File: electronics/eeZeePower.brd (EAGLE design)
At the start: 20.3 x 11.6 mm, 10 parts

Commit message: Updated version #
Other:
- board text added: "R0.6"
- board text removed: "R0.5"
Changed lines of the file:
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@@
 <text x="5.334" y="1.651" size="1.27" layer="27" font="vector">eeZee Power</text>
 <text x="5.334" y="0.508" size="1.016" layer="21" font="vector">bot-thoughts.com</text>
-<text x="19.939" y="4.318" size="0.8128" layer="21" font="vector" rot="R90">R0.5</text>
+<text x="19.939" y="4.318" size="0.8128" layer="21" font="vector" rot="R90">R0.6</text>
 <text x="11.176" y="7.493" size="1.016" layer="27" font="vector" rot="R180">VCC</text>
 <text x="11.176" y="4.953" size="1.016" layer="27" font="vector" rot="R180">GND</text>

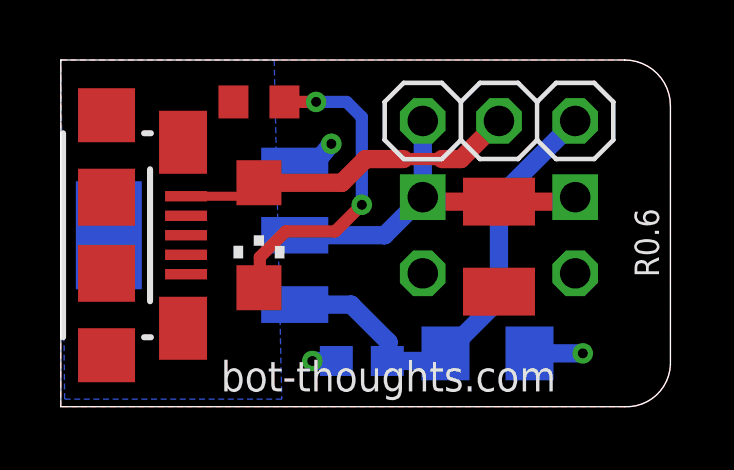
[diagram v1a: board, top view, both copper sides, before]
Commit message: updated silk, updated board name to microB
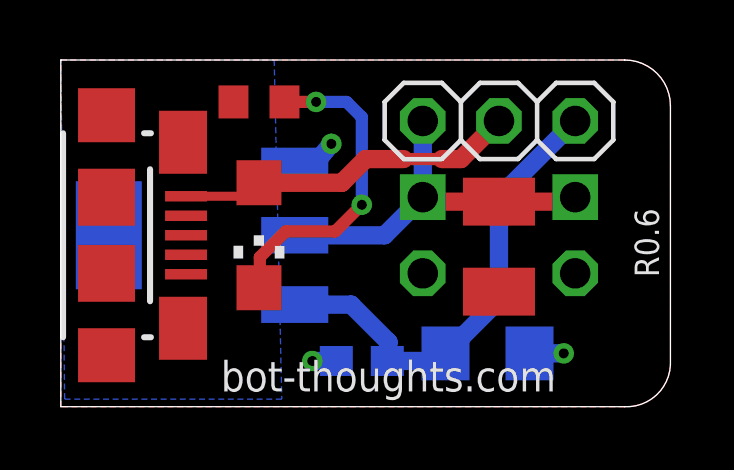
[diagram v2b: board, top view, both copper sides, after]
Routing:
- net GND: track 4.14 -> 3.51 mm
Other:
- board text added: "eeZeePowerμB"
- board text removed: "eeZee Power"
- board text removed: "μB"
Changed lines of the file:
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@@
 <wire x1="0" y1="11.557" x2="0" y2="0" width="0" layer="20"/>
 <text x="10.541" y="8.636" size="1.016" layer="27" font="vector" rot="R90">VU</text>
-<text x="5.334" y="1.651" size="1.27" layer="27" font="vector">eeZee Power</text>
+<text x="5.334" y="1.651" size="1.27" layer="27" font="vector">eeZeePowerμB</text>
 <text x="5.334" y="0.508" size="1.016" layer="21" font="vector">bot-thoughts.com</text>
 <text x="19.939" y="4.318" size="0.8128" layer="21" font="vector" rot="R90">R0.6</text>
@@
 <text x="11.176" y="4.953" size="1.016" layer="27" font="vector" rot="R180">GND</text>
 <text x="18.669" y="10.795" size="1.016" layer="27" font="vector" rot="R270">3V3</text>
-<text x="17.907" y="1.778" size="1.27" layer="27" font="vector">μB</text>
 </plain>
 <attributes>
@@
 <contactref element="JP1" pad="GND"/>
 <wire x1="9.183" y1="1.524" x2="8.382" y2="1.524" width="0.6096" layer="16"/>
-<wire x1="15.624" y1="1.778" x2="17.399" y2="1.778" width="0.6096" layer="16"/>
+<wire x1="15.624" y1="1.778" x2="16.764" y2="1.778" width="0.6096" layer="16"/>
 <via x="8.382" y="1.524" extent="1-16" drill="0.3302"/>
-<via x="17.399" y="1.778" extent="1-16" drill="0.3302"/>
+<via x="16.764" y="1.778" extent="1-16" drill="0.3302"/>
 <wire x1="7.7978" y1="8.0264" x2="8.4074" y2="8.0264" width="0.6096" layer="16"/>
 <wire x1="8.4074" y1="8.0264" x2="9.017" y2="8.763" width="0.6096" layer="16"/>
